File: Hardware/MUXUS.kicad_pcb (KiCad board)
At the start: 4 copper layers, 99.1 x 99.1 mm, 120 parts, among them J1 USB_C_Receptacle_USB2.0, J2 USB_B, J3 USB_A, J4 USB_B, J5 USB_A, J6 STDC14, J7 USB_B, J8 USB_A, SW1 USER, SW2 RESET, U1 USBLC6-4SC6, U10 AP2151W, U11 AOZ1212AI, U12 USBLC6-2SC6, U13 USBLC6-2SC6, U14 AP2151W, U2 USB2504A-JT, U3 USBLC6-2SC6, U4 USBLC6-2SC6, U5 AP2151W, U6 TS3USBCA420RSVR, U7 STM32G431K8T6, U8 USBLC6-2SC6, U9 USBLC6-2SC6, Y1 ATS240C

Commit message: Basic routing
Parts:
- moved R24 41.3 mm to (97.5, 52.1), turned to 90 degrees
- moved R15 17.9 mm to (97.5, 72.4), turned to 90 degrees
- moved C18 0.38 mm to (94.2, 90.2)
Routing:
- net GND: track 0.00 -> 50.5 mm, vias 0 -> 2
- net +3V3: track 0.00 -> 29.0 mm, vias 0 -> 5
- net UFP1_VBUS: track 0.00 -> 22.9 mm, vias 0 -> 2
- net Net-(C34-Pad2): track 0.00 -> 21.9 mm
- net Net-(C36-Pad1): track 0.00 -> 14.2 mm
- net Net-(C24-Pad1): track 0.00 -> 14.2 mm
- net Net-(C14-Pad1): track 0.00 -> 14.2 mm
- net Net-(C2-Pad2): track 0.00 -> 13.5 mm
- net Net-(C1-Pad1): track 0.00 -> 13.4 mm
- net Net-(C30-Pad2): track 0.00 -> 11.6 mm
- net Net-(C13-Pad2): track 0.00 -> 10.8 mm
- net Net-(C23-Pad2): track 0.00 -> 10.8 mm
- net Net-(C35-Pad2): track 0.00 -> 10.7 mm
- net BOOT0: track 0.00 -> 8.05 mm
- net NRST: track 0.00 -> 8.05 mm
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- added copper zone on In2.Cu, net +3V3
- added copper zone on In1.Cu, net GND

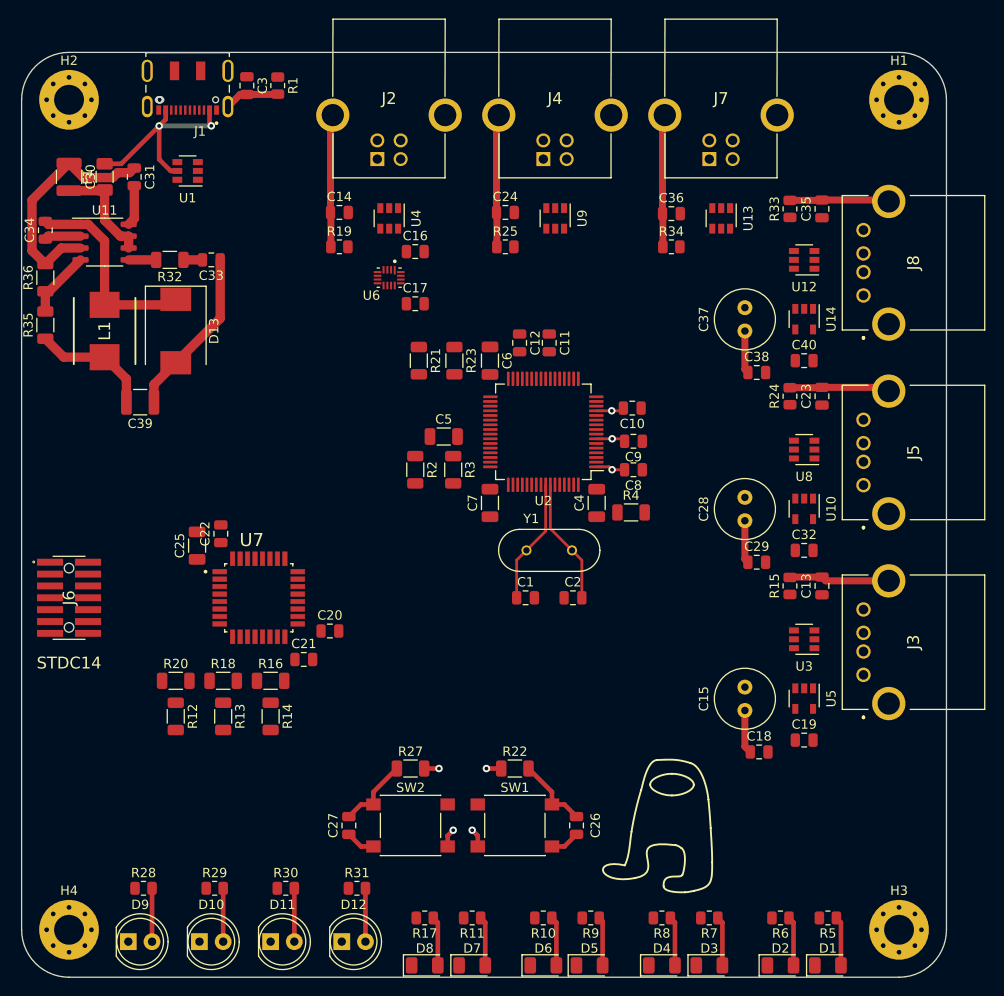
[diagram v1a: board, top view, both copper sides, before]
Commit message: First PCB routing
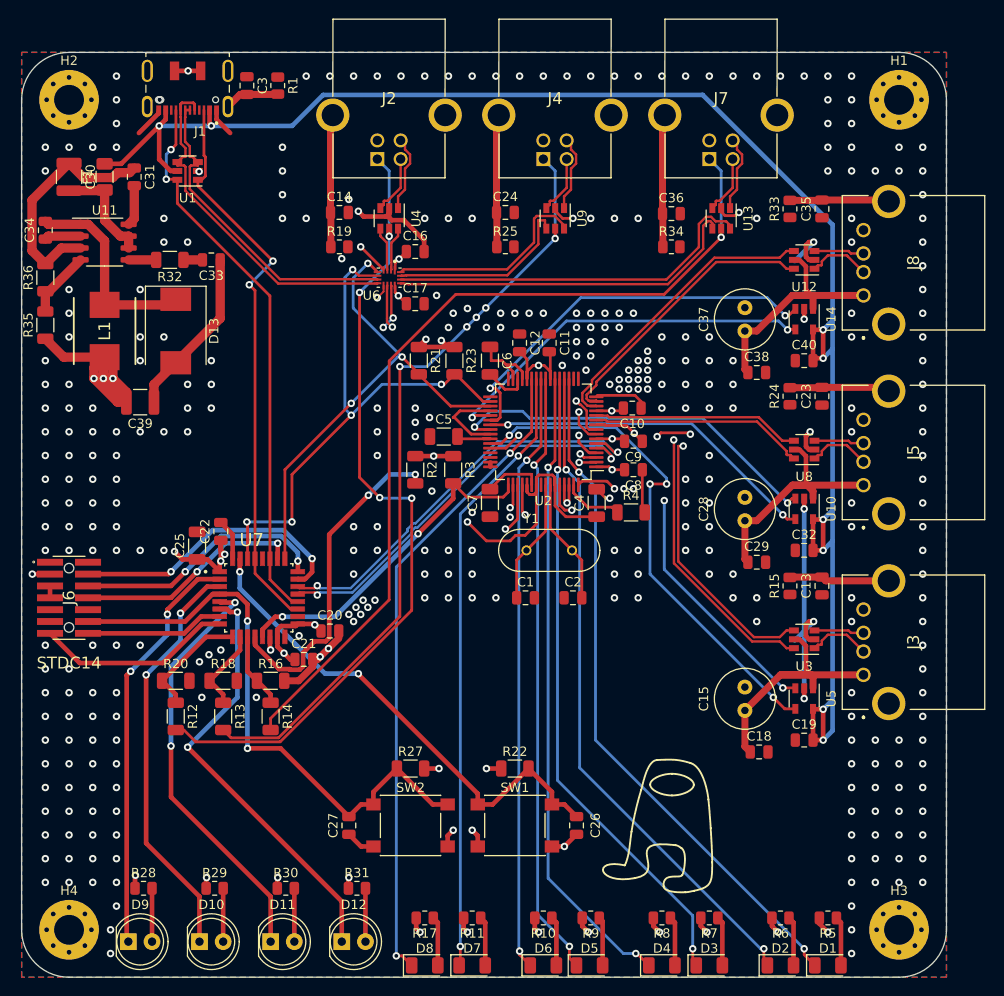
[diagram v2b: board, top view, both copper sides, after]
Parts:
- moved C22 0.25 mm to (36.6, 66.5)
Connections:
- C5 pad 2: Net-(C4-Pad2) -> Net-(C5-Pad2)
- C6 pad 2: Net-(C4-Pad2) -> Net-(C6-Pad2)
- C7 pad 2: Net-(C4-Pad2) -> Net-(C7-Pad2)
- U1 pad 3: UFP1_D- -> UFP1_D+
- U1 pad 4: UFP1_D+ -> UFP1_D-
- U2 pad 30: Net-(C4-Pad2) -> Net-(C6-Pad2)
- U2 pad 42: Net-(C4-Pad2) -> Net-(C5-Pad2)
- U2 pad 54: Net-(C4-Pad2) -> Net-(C7-Pad2)
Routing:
- net UFP1_VBUS: track 22.9 -> 185.7 mm, vias 2 -> 8
- net GND: track 50.5 -> 209.9 mm, vias 2 -> 356
- net +3V3: track 29.0 -> 125.1 mm, vias 5 -> 37
- net UFP4_VBUS: track 0.00 -> 95.7 mm, vias 0 -> 1
- net UFP2_VBUS: track 0.00 -> 86.9 mm, vias 0 -> 4
- net UFP3_VBUS: track 0.00 -> 83.8 mm, vias 0 -> 5
- net Net-(D1-Pad1): track 0.00 -> 73.7 mm, vias 0 -> 2
- net Net-(D2-Pad1): track 0.00 -> 72.0 mm, vias 0 -> 2
- net Net-(D8-Pad1): track 0.00 -> 69.9 mm, vias 0 -> 2
- net Net-(D3-Pad1): track 0.00 -> 69.1 mm, vias 0 -> 2
- net Net-(D4-Pad1): track 0.00 -> 68.5 mm, vias 0 -> 2
- net Net-(D7-Pad1): track 0.00 -> 66.3 mm, vias 0 -> 2
- net Net-(D5-Pad1): track 0.00 -> 65.2 mm, vias 0 -> 2
- net Net-(D6-Pad1): track 0.00 -> 64.3 mm, vias 0 -> 2
- net CC1: track 0.00 -> 61.1 mm, vias 0 -> 2
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- added copper zone on B.Cu, net GND
- added copper zone on F.Cu, net GND
- added copper zone on In1.Cu, net Net-(C13-Pad2)
- added copper zone on In1.Cu, net Net-(C14-Pad1)
- added copper zone on In1.Cu, net Net-(C23-Pad2)
- added copper zone on In1.Cu, net Net-(C24-Pad1)
- added copper zone on In1.Cu, net Net-(C3-Pad2)
- added copper zone on In1.Cu, net Net-(C35-Pad2)
- added copper zone on In1.Cu, net Net-(C36-Pad1)
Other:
- net class Default: clearance 0.2 -> 0.127
- rule trace_clearance: 0.2 -> 0.127

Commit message: Add labels on silkscreen
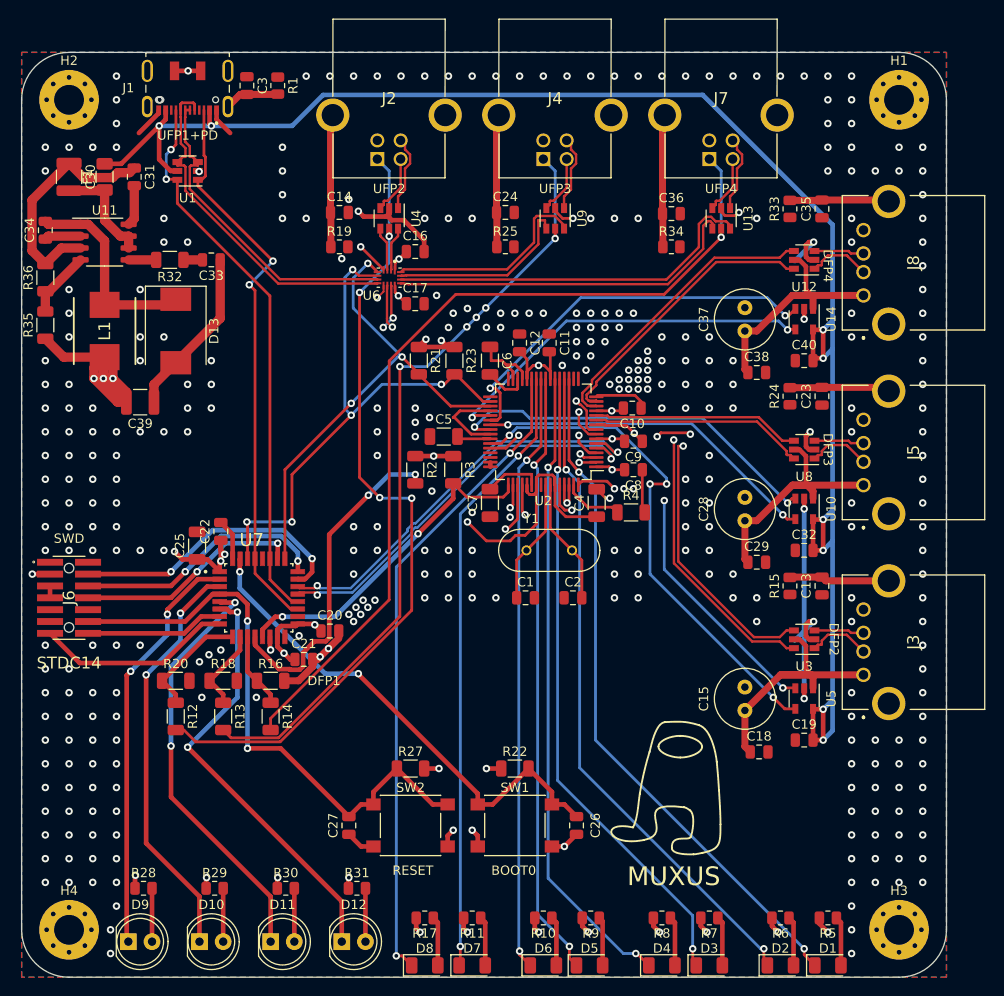
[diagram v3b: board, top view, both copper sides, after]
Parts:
- moved SYM1 4.16 mm to (85.7, 94.0)
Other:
- board text added: "BOOT0"
- board text added: "DFP1"
- board text added: "DFP2"
- board text added: "DFP3"
- board text added: "DFP4"
- board text added: "MUXUS"
- board text added: "RESET"
- board text added: "SWD"
- board text added: "UFP1+PD"
- board text added: "UFP2"
- board text added: "UFP3"
- board text added: "UFP4"

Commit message: DEBUG connectors and VIAS
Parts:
- added J10: VCP, Connector_PinHeader_2.54mm:PinHeader_1x02_P2.54mm_Vertical, F.Cu at (20.3, 99.1)
- added J9: SWD, Connector_PinHeader_2.54mm:PinHeader_1x06_P2.54mm_Vertical, F.Cu at (20.3, 81.3)
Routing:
- net SWO: track 24.4 -> 53.2 mm
- net SWDIO: track 30.5 -> 58.2 mm
- net LPUART1_RX: track 21.2 -> 46.5 mm
- net LPUART1_TX: track 14.9 -> 37.7 mm, vias 0 -> 1
- net NRST: track 63.2 -> 83.0 mm
- net SWCLK: track 27.5 -> 46.3 mm
- net GND: track 209.9 -> 214.9 mm, vias 356 -> 645
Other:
- board text added: "3.3V"
- board text added: "GND"
- board text added: "NRST"
- board text added: "RX"
- board text added: "SWCLK"
- board text added: "SWDIO"
- board text added: "SWO"
- board text added: "TX"
- board text removed: "SWD"

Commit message: JLCJLCJLCJLC
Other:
- board text added: "JLCJLCJLCJLC"
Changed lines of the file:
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@@
   (general
     (thickness 1.6)
-    (drawings 27)
+    (drawings 28)
     (tracks 1879)
     (zones 0)
@@
       (net 3 "Net-(C2-Pad2)"))
   )
+  (gr_text JLCJLCJLCJLC (at 71.12 54.61) (layer F.SilkS)
+    (effects (font (size 0.889 0.889) (thickness 0.127)))
+  )
   (gr_text RX (at 21.59 101.6) (layer F.SilkS)

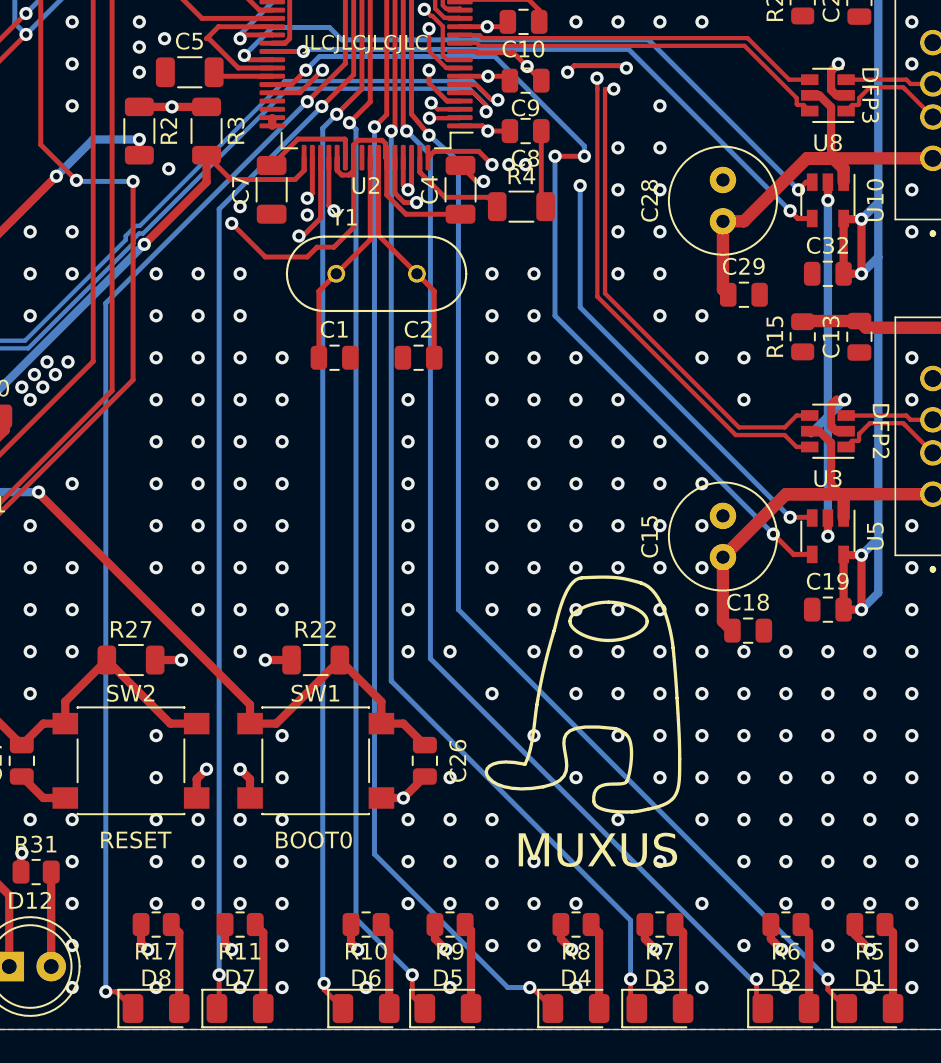
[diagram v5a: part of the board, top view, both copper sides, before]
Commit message: Repair via gaps
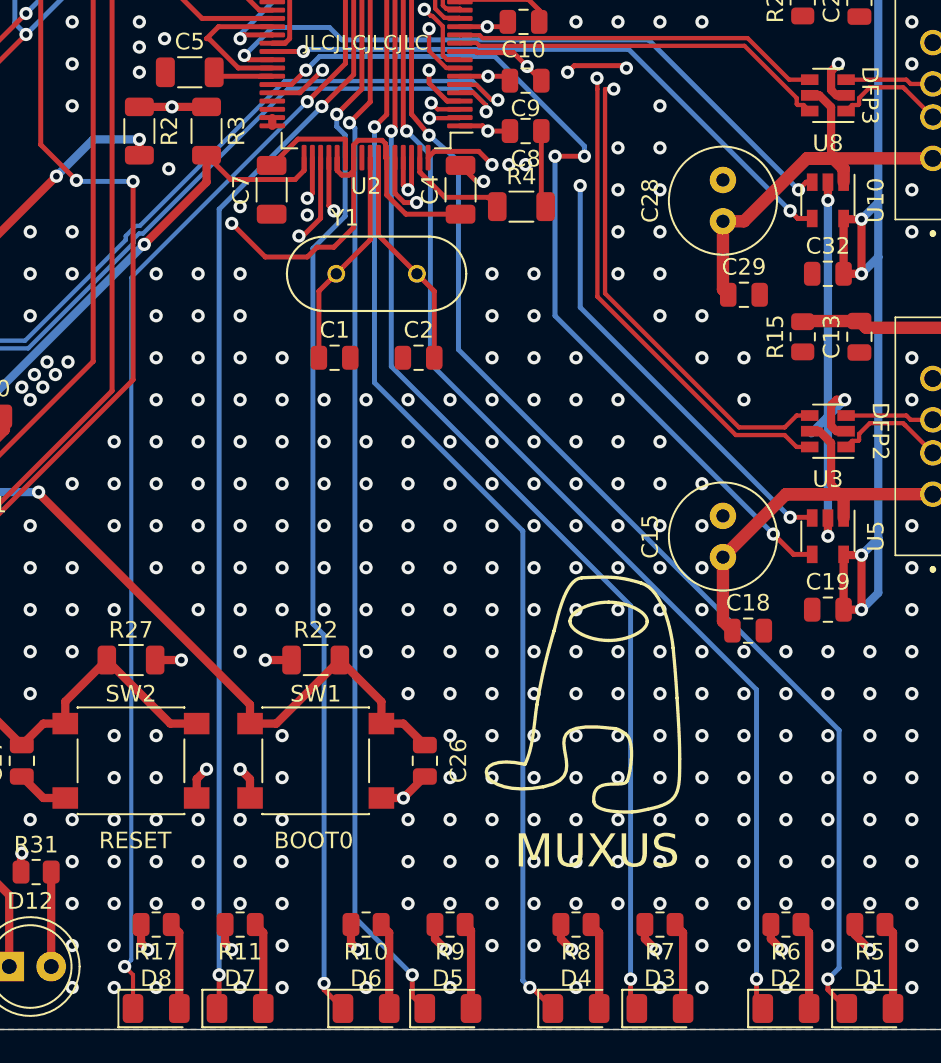
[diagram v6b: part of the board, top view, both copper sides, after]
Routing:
- net Net-(D8-Pad1): track 69.9 -> 68.6 mm
- net Net-(D6-Pad1): track 64.3 -> 65.3 mm
- net Net-(D4-Pad1): track 68.5 -> 67.7 mm
- net Net-(D1-Pad1): track 73.7 -> 74.3 mm
- net GND: vias 645 -> 694
- net (no net): vias 2 -> 3

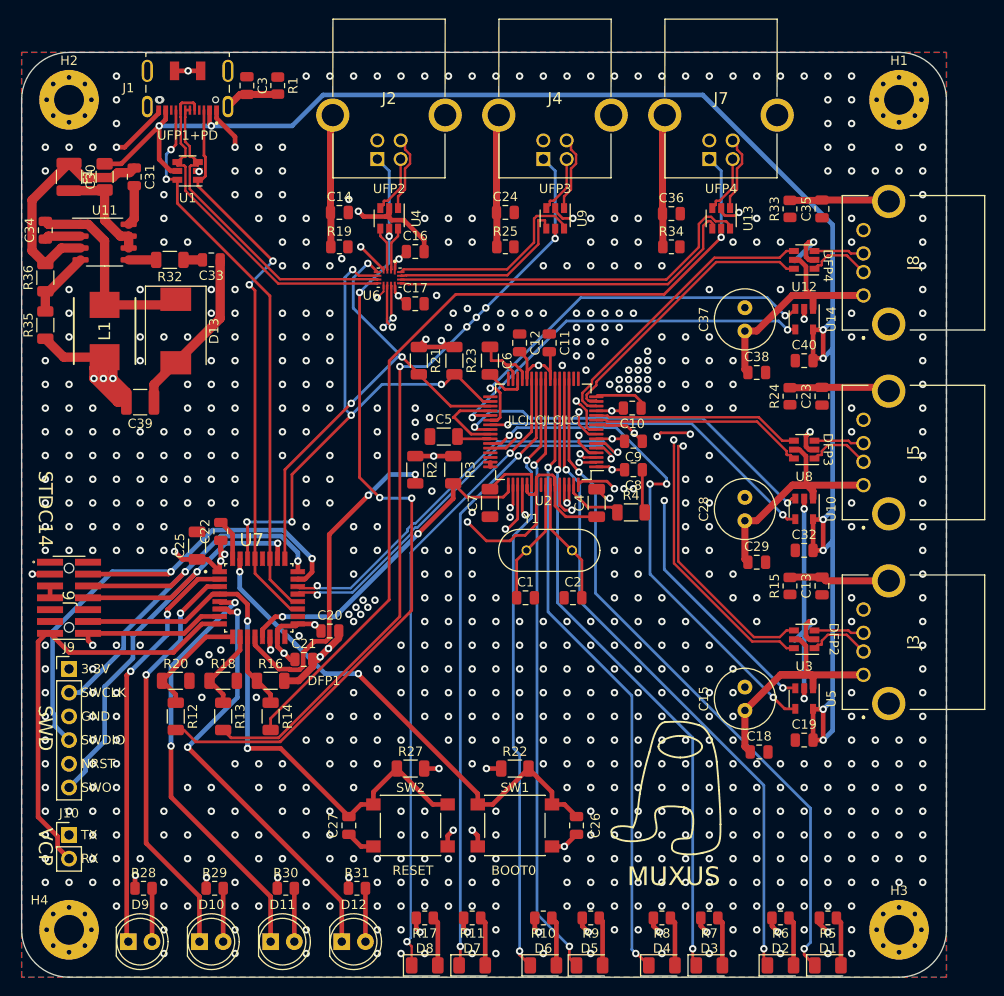
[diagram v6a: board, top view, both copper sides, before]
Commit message: Measure UFP1_VBUS as well for the UCPD stack
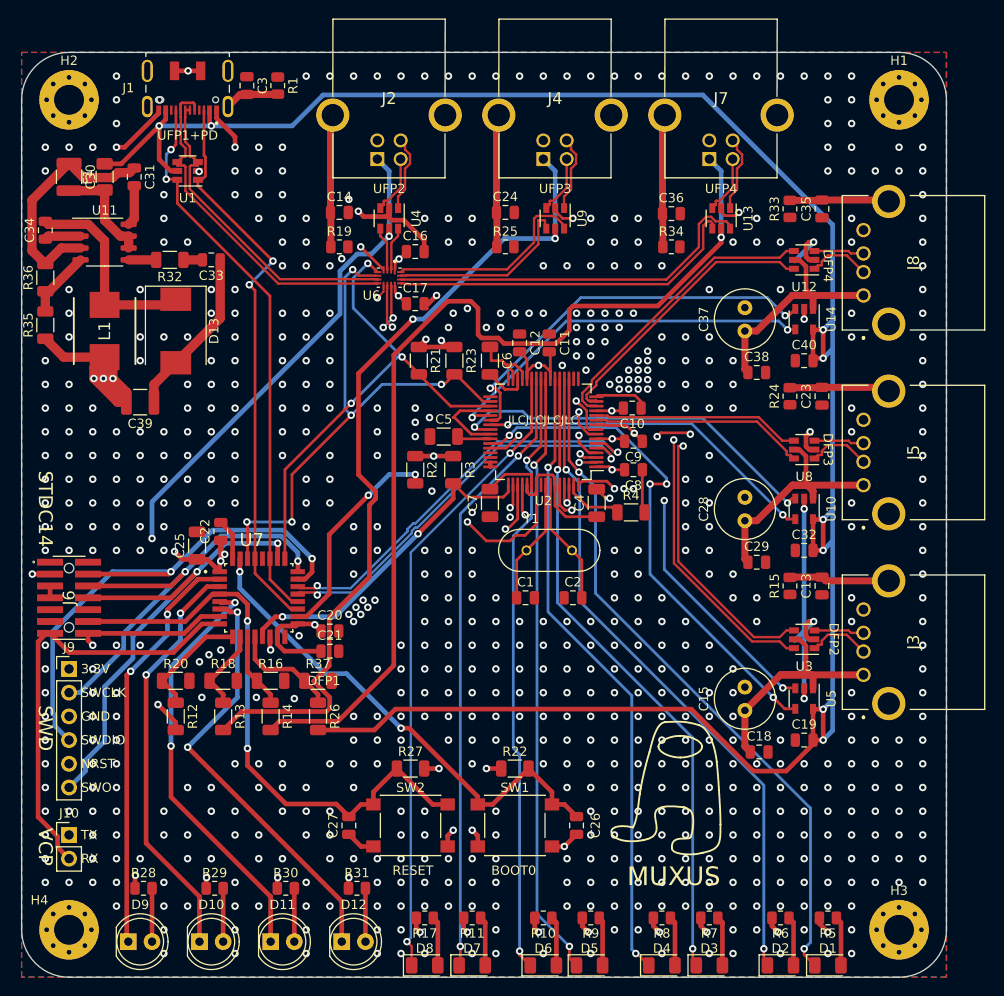
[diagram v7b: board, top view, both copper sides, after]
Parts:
- added R26: 10K, Resistor_SMD:R_1206_3216Metric, F.Cu at (47.0, 86.4)
- added R37: 1K, Resistor_SMD:R_1206_3216Metric, F.Cu at (47.0, 82.5)
- moved C21 2.93 mm to (48.3, 79.4)
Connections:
- U7 pad 12: IFP_VBUS -> Net-(R26-Pad1)
- U7 pad 18: Net-(U7-Pad18) -> IFP_VBUS
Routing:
- net UFP1_VBUS: track 185.7 -> 244.1 mm
- net IFP_VBUS: track 53.3 -> 40.8 mm
- net UFP2_VBUS: track 86.9 -> 75.0 mm, vias 4 -> 3
- net Net-(R26-Pad1): track 0.00 -> 11.6 mm
- net UFP4_VBUS: track 95.7 -> 106.5 mm
- net GND: track 214.9 -> 207.6 mm, vias 694 -> 692
- net UFP3_VBUS: track 83.8 -> 89.6 mm, vias 5 -> 2
- net +3V3: track 125.1 -> 127.3 mm, vias 37 -> 36
- net NRST: track 83.0 -> 84.0 mm
